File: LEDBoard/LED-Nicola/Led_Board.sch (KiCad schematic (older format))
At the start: 33 parts, among them J1 MOUNTING_HOLE, J10 CONN_01X02, J11 LED CONN 01X16, J12 CONN_01X02, J13 LED CONN 01X04, J2 MOUNTING_HOLE, J3 MOUNTING_HOLE, J4 MOUNTING_HOLE, J5 Arduino CONN 01X04, J6 Arduino CONN_01X04, J7 Arduino CONN_01X06, J8 VD 0 CONN_01X02, J9 CONN_01X02, Q1 MMBT2222ALT1G, U1 SSR

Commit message: Changes
plz let me push
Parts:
- added BZ101: Buzzer, hyperCustom:nicolaBuzzer, symbol Buzzer
- added R101, R102: R, Resistors_ThroughHole:R_Axial_DIN0309_L9.0mm_D3.2mm_P12.70mm_Horizontal, symbol R
- J11: Digikey PN (none) -> 277-1220-ND; Link (none) -> https://www.digikey.com/product-detail/en/phoenix-contact/1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
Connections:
- net 5V0: now also R102.2
- net Buzzer: now also R101.1; no longer U1.5 (LOAD)
- net GND: now also BZ101.2 (+)
- new net: R101.2, U1.5 (LOAD)
- new net: BZ101.1 (-), R102.1
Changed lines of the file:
@@
 LIBS:contrib
 LIBS:valves
-LIBS:KiCAD_Tutorial
-LIBS:5vregulatortab
-LIBS:ssr
-LIBS:SSRBoard-cache
-LIBS:SSRBoard-rescue
-LIBS:Arduino_Uno_R3_From_Scratch
-LIBS:Arduino_Uno_R3_From_Scratch-cache
-LIBS:MFN_Atmel
-LIBS:xtr117
-LIBS:mmbt2222alt1g
-LIBS:VO14642AABTR
 LIBS:Led_Board-cache
 EELAYER 25 0
@@
 F 2 "hyperCustom:CONN_PHOENIX_1844359_16PIN" H 9100 2900 50  0001 C CNN
 F 3 "" H 9100 2900 50  0001 C CNN
+F 4 "277-1220-ND" H 9100 2900 60  0001 C CNN "Digikey PN"
+F 5 "https://www.digikey.com/product-detail/en/phoenix-contact/1803413/277-1220-ND/260588" H 9100 2900 60  0001 C CNN "Link"
 	1    9100 2900
 	0    -1   -1   0
@@
 Text Label 7400 850  0    60   ~ 0
 24V
-Text Label 7450 1000 0    60   ~ 0
+Text Label 7750 1000 0    60   ~ 0
 Buzzer
 Text Label 7950 1600 2    60   ~ 0
@@
 Text Label 5950 850  2    60   ~ 0
 5V0
+$Comp
+L Buzzer BZ101
+U 1 1 597D61D1
+P 1600 5200
+F 0 "BZ101" H 1750 5250 50  0000 L CNN
+F 1 "Buzzer" H 1750 5150 50  0000 L CNN
+F 2 "hyperCustom:nicolaBuzzer" V 1575 5300 50  0001 C CNN
+F 3 "" V 1575 5300 50  0001 C CNN
+F 4 "http://www.puiaudio.com/pdf/AI-3035-TWT-3V-R.pdf" H 1600 5200 60  0001 C CNN "Link"
+	1    1600 5200
+	1    0    0    -1
+$EndComp
+Text Label 1050 5100 2    60   ~ 0
+5V0
+$Comp
+L GND #PWR101
+U 1 1 597D688D
+P 1500 5300
+F 0 "#PWR101" H 1500 5050 50  0001 C CNN
+F 1 "GND" H 1500 5150 50  0000 C CNN
+F 2 "" H 1500 5300 50  0001 C CNN
+F 3 "" H 1500 5300 50  0001 C CNN
+	1    1500 5300
+	1    0    0    -1
+$EndComp
+$Comp
+L R R102
+U 1 1 597D6C18
+P 1350 5100
+F 0 "R102" V 1430 5100 50  0000 C CNN
+F 1 "R" V 1350 5100 50  0000 C CNN
+F 2 "Resistors_ThroughHole:R_Axial_DIN0309_L9.0mm_D3.2mm_P12.70mm_Horizontal" V 1280 5100 50  0001 C CNN
+F 3 "" H 1350 5100 50  0001 C CNN
+	1    1350 5100
+	0    1    1    0
+$EndComp
+Wire Wire Line
+	1200 5100 1050 5100
+$Comp
+L R R101
+U 1 1 597D728C
+P 7600 1000
+F 0 "R101" V 7680 1000 50  0000 C CNN
+F 1 "R" V 7600 1000 50  0000 C CNN
+F 2 "Resistors_ThroughHole:R_Axial_DIN0309_L9.0mm_D3.2mm_P12.70mm_Horizontal" V 7530 1000 50  0001 C CNN
+F 3 "" H 7600 1000 50  0001 C CNN
+	1    7600 1000
+	0    1    1    0
+$EndComp
 $EndSCHEMATC

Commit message: new changes
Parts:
- removed BZ101: Buzzer, hyperCustom:nicolaBuzzer, symbol Buzzer
- removed R101, R102: R, Resistors_ThroughHole:R_Axial_DIN0309_L9.0mm_D3.2mm_P12.70mm_Horizontal, symbol R
- J11: Digikey PN 277-1220-ND -> (none); Link https://www.digikey.com/product-detail/en/phoenix-contact/1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 -> (none)
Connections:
- net Buzzer: now also U1.5 (LOAD)
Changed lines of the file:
@@
 LIBS:contrib
 LIBS:valves
+LIBS:KiCAD_Tutorial
+LIBS:5vregulatortab
+LIBS:ssr
+LIBS:SSRBoard-cache
+LIBS:SSRBoard-rescue
+LIBS:Arduino_Uno_R3_From_Scratch
+LIBS:Arduino_Uno_R3_From_Scratch-cache
+LIBS:MFN_Atmel
+LIBS:xtr117
+LIBS:mmbt2222alt1g
+LIBS:VO14642AABTR
 LIBS:Led_Board-cache
 EELAYER 25 0
@@
 F 2 "hyperCustom:CONN_PHOENIX_1844359_16PIN" H 9100 2900 50  0001 C CNN
 F 3 "" H 9100 2900 50  0001 C CNN
-F 4 "277-1220-ND" H 9100 2900 60  0001 C CNN "Digikey PN"
-F 5 "https://www.digikey.com/product-detail/en/phoenix-contact/1803413/277-1220-ND/260588" H 9100 2900 60  0001 C CNN "Link"
 	1    9100 2900
 	0    -1   -1   0
@@
 Text Label 7400 850  0    60   ~ 0
 24V
-Text Label 7750 1000 0    60   ~ 0
+Text Label 7450 1000 0    60   ~ 0
 Buzzer
 Text Label 7950 1600 2    60   ~ 0
@@
 Text Label 5950 850  2    60   ~ 0
 5V0
-$Comp
-L Buzzer BZ101
-U 1 1 597D61D1
-P 1600 5200
-F 0 "BZ101" H 1750 5250 50  0000 L CNN
-F 1 "Buzzer" H 1750 5150 50  0000 L CNN
-F 2 "hyperCustom:nicolaBuzzer" V 1575 5300 50  0001 C CNN
-F 3 "" V 1575 5300 50  0001 C CNN
-F 4 "http://www.puiaudio.com/pdf/AI-3035-TWT-3V-R.pdf" H 1600 5200 60  0001 C CNN "Link"
-	1    1600 5200
-	1    0    0    -1
-$EndComp
-Text Label 1050 5100 2    60   ~ 0
-5V0
-$Comp
-L GND #PWR101
-U 1 1 597D688D
-P 1500 5300
-F 0 "#PWR101" H 1500 5050 50  0001 C CNN
-F 1 "GND" H 1500 5150 50  0000 C CNN
-F 2 "" H 1500 5300 50  0001 C CNN
-F 3 "" H 1500 5300 50  0001 C CNN
-	1    1500 5300
-	1    0    0    -1
-$EndComp
-$Comp
-L R R102
-U 1 1 597D6C18
-P 1350 5100
-F 0 "R102" V 1430 5100 50  0000 C CNN
-F 1 "R" V 1350 5100 50  0000 C CNN
-F 2 "Resistors_ThroughHole:R_Axial_DIN0309_L9.0mm_D3.2mm_P12.70mm_Horizontal" V 1280 5100 50  0001 C CNN
-F 3 "" H 1350 5100 50  0001 C CNN
-	1    1350 5100
-	0    1    1    0
-$EndComp
-Wire Wire Line
-	1200 5100 1050 5100
-$Comp
-L R R101
-U 1 1 597D728C
-P 7600 1000
-F 0 "R101" V 7680 1000 50  0000 C CNN
-F 1 "R" V 7600 1000 50  0000 C CNN
-F 2 "Resistors_ThroughHole:R_Axial_DIN0309_L9.0mm_D3.2mm_P12.70mm_Horizontal" V 7530 1000 50  0001 C CNN
-F 3 "" H 7600 1000 50  0001 C CNN
-	1    7600 1000
-	0    1    1    0
-$EndComp
 $EndSCHEMATC

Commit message: changes
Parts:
- added BZ101: Buzzer, hyperCustom:nicolaBuzzer, symbol Buzzer
- added R101, R102: R, Resistors_ThroughHole:R_Axial_DIN0309_L9.0mm_D3.2mm_P12.70mm_Horizontal, symbol R
- J10: DigiKey PN (none) -> 277-2416-ND; Mfg.  (none) -> Phoenix; Mfg. PN (none) -> 1844210
- J11: Digikey PN (none) -> 277-6211-ND; Link (none) -> https://www.digikey.com/product-detail/en/phoenix-contact/1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; Mfg.  (none) -> Phoenix; Mfg. PN (none) -> 1828003
- J12: Digikey PN (none) -> 277-2416-ND; Mfg.  (none) -> Phoenix; Mfg. PN (none) -> 1844210
- J13, J5, J6: Digikey PN (none) -> 277-2419-ND; Mfg.  (none) -> Phoenix; Mfg. PN (none) -> 1844236
- J7: Digikey PN (none) -> 277-2427-ND; Mfg.  (none) -> Phoenix; Mfg. PN (none) -> 1844525
- J8, J9: Digikey PN (none) -> 277-2416-ND; Mfg. (none) -> Phoenix; Mfg. PN (none) -> 1844210
- Q1: Mfg. (none) -> ON Semiconductors
- U1: Digikey PN (none) -> VO14642AABCT-ND; Mfg (none) -> Vishay Semiconductor Oppto Division; Mfg. PN (none) -> VO14642AABTR
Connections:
- net 24V: now also J5.2 (P2); no longer J5.3 (P3)
- net 5V0: now also J5.3 (P3); no longer J5.4 (P4)
- net A0: now also J5.1 (P1); no longer J5.2 (P2)
- net A1: now also J6.4 (P4); no longer J5.1 (P1)
- net A2: now also J6.3 (P3); no longer J6.4 (P4)
- net A3: now also J6.2 (P2); no longer J6.3 (P3)
- net A4: now also J6.1 (P1); no longer J6.2 (P2)
- net A5: now also J7.6 (P6); no longer J6.1 (P1)
- net A6: now also J7.5 (P5); no longer J7.6 (P6)
- net A7: now also J7.4 (P4); no longer J7.5 (P5), Q1.1 (B)
- net A8: now also J7.3 (P3); no longer J7.4 (P4)
- net Buzzer: now also R101.1; no longer U1.5 (LOAD)
- net GND: now also BZ101.2 (+); no longer J7.2 (P2)
- net ArduinoLED: now reaches J7.1 (P1)
- net ArduinoLED: now also R17.2
- removed net A9: J7.3 (P3), R17.2
- new net: R101.2, U1.5 (LOAD)
- new net: BZ101.1 (-), R102.1
- new net 5V: J7.2 (P2), R102.2
- new net Transistor: J5.4 (P4), Q1.1 (B)
- no-connect marks 3 -> 2
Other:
- moved on the sheet: J5, J6, J7
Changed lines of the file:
@@
 F 2 "VO14642AABTR:SOIC254P1005X390-6N" H 6700 1000 60  0001 C CNN
 F 3 "" H 6700 1000 60  0001 C CNN
+F 4 "VO14642AABCT-ND" H 6700 1000 60  0001 C CNN "Digikey PN"
+F 5 "Vishay Semiconductor Oppto Division" H 6700 1000 60  0001 C CNN "Mfg"
+F 6 "VO14642AABTR" H 6700 1000 60  0001 C CNN "Mfg. PN"
 	1    6700 1000
 	1    0    0    -1
@@
 GND
 Text Label 5300 1350 3    60   ~ 0
-A7
+Transistor
 $Comp
 L R R7
@@
 Text Label 2850 2950 0    60   ~ 0
 A6
-Text Label 2850 3050 0    60   ~ 0
-A7
+Text Label 2600 2050 0    60   ~ 0
+Transistor
 Wire Wire Line
 	2600 3050 2850 3050
@@
 L CONN_01X04 J5
 U 1 1 5979ADB2
-P 2400 2300
-F 0 "J5" H 2500 2250 50  0000 C CNN
-F 1 "Arduino CONN 01X04" H 2850 2150 50  0000 C CNN
-F 2 "hyperCustom:CONN_PHOENIX_1844236_4PIN" H 2400 2300 50  0001 C CNN
-F 3 "" H 2400 2300 50  0001 C CNN
-	1    2400 2300
+P 2400 2200
+F 0 "J5" H 2500 2150 50  0000 C CNN
+F 1 "Arduino CONN 01X04" H 2850 2050 50  0000 C CNN
+F 2 "hyperCustom:CONN_PHOENIX_1844236_4PIN" H 2400 2200 50  0001 C CNN
+F 3 "" H 2400 2200 50  0001 C CNN
+F 4 "277-2419-ND" H 2400 2200 60  0001 C CNN "Digikey PN"
+F 5 "Phoenix" H 2400 2200 60  0001 C CNN "Mfg. "
+F 6 "1844236" H 2400 2200 60  0001 C CNN "Mfg. PN"
+	1    2400 2200
 	-1   0    0    1
 $EndComp
@@
 L CONN_01X04 J6
 U 1 1 5979AE62
-P 2400 2700
-F 0 "J6" H 2500 2650 50  0000 C CNN
-F 1 "Arduino CONN_01X04" H 2850 2550 50  0000 C CNN
-F 2 "hyperCustom:CONN_PHOENIX_1844236_4PIN" H 2400 2700 50  0001 C CNN
-F 3 "" H 2400 2700 50  0001 C CNN
-	1    2400 2700
+P 2400 2600
+F 0 "J6" H 2500 2550 50  0000 C CNN
+F 1 "Arduino CONN_01X04" H 2850 2450 50  0000 C CNN
+F 2 "hyperCustom:CONN_PHOENIX_1844236_4PIN" H 2400 2600 50  0001 C CNN
+F 3 "" H 2400 2600 50  0001 C CNN
+F 4 "277-2419-ND" H 2400 2600 60  0001 C CNN "Digikey PN"
+F 5 "Phoenix" H 2400 2600 60  0001 C CNN "Mfg. "
+F 6 "1844236" H 2400 2600 60  0001 C CNN "Mfg. PN"
+	1    2400 2600
 	-1   0    0    1
 $EndComp
@@
 F 2 "hyperCustom:CONN_PHOENIX_1844210_2PIN" H 4050 4850 50  0001 C CNN
 F 3 "" H 4050 4850 50  0001 C CNN
+F 4 "277-2416-ND" H 4050 4850 60  0001 C CNN "Digikey PN"
+F 5 "Phoenix" H 4050 4850 60  0001 C CNN "Mfg."
+F 6 "1844210" H 4050 4850 60  0001 C CNN "Mfg. PN"
 	1    4050 4850
 	0    -1   -1   0
@@
 F 2 "hyperCustom:CONN_PHOENIX_1844210_2PIN" H 4800 4850 50  0001 C CNN
 F 3 "" H 4800 4850 50  0001 C CNN
+F 4 "277-2416-ND" H 4800 4850 60  0001 C CNN "Digikey PN"
+F 5 "Phoenix" H 4800 4850 60  0001 C CNN "Mfg."
+F 6 "1844210" H 4800 4850 60  0001 C CNN "Mfg. PN"
 	1    4800 4850
 	0    -1   -1   0
@@
 F 2 "hyperCustom:CONN_PHOENIX_1844210_2PIN" H 5400 4850 50  0001 C CNN
 F 3 "" H 5400 4850 50  0001 C CNN
+F 4 "277-2416-ND" H 5400 4850 60  0001 C CNN "DigiKey PN"
+F 5 "Phoenix" H 5400 4850 60  0001 C CNN "Mfg. "
+F 6 "1844210" H 5400 4850 60  0001 C CNN "Mfg. PN"
 	1    5400 4850
 	0    -1   -1   0
@@
 Wire Wire Line
 	2600 3250 2850 3250
-Text Label 2850 3350 0    60   ~ 0
-GND
 Wire Wire Line
 	7650 4500 7650 4250
@@
 F 2 "hyperCustom:CONN_PHOENIX_1844359_16PIN" H 9100 2900 50  0001 C CNN
 F 3 "" H 9100 2900 50  0001 C CNN
+F 4 "277-6211-ND" H 9100 2900 60  0001 C CNN "Digikey PN"
+F 5 "https://www.digikey.com/product-detail/en/phoenix-contact/1803413/277-1220-ND/260588" H 9100 2900 60  0001 C CNN "Link"
+F 6 "Phoenix" H 9100 2900 60  0001 C CNN "Mfg. "
+F 7 "1828003" H 9100 2900 60  0001 C CNN "Mfg. PN"
 	1    9100 2900
 	0    -1   -1   0
@@
 F 2 "foot:MMBF170LT1G" H 5700 1350 60  0001 C CNN
 F 3 "" H 5700 1350 60  0000 C CNN
+F 4 "ON Semiconductors" H 5700 1350 60  0001 C CNN "Mfg."
 	1    5700 1350
 	1    0    0    -1
@@
 F 2 "hyperCustom:CONN_PHOENIX_1844210_2PIN" H 8400 1650 50  0001 C CNN
 F 3 "" H 8400 1650 50  0001 C CNN
+F 4 "277-2416-ND" V 8400 1650 60  0001 C CNN "Digikey PN"
+F 5 "Phoenix" V 8400 1650 60  0001 C CNN "Mfg. "
+F 6 "1844210" V 8400 1650 60  0001 C CNN "Mfg. PN"
 	1    8400 1650
 	1    0    0    -1
@@
 A8
 $Comp
-L R R17
-U 1 1 597CFDDB
-P 9800 4650
-F 0 "R17" V 9880 4650 50  0000 C CNN
-F 1 "220" V 9800 4650 50  0000 C CNN
-F 2 "Resistors_SMD:R_1206_HandSoldering" V 9730 4650 50  0001 C CNN
-F 3 "" H 9800 4650 50  0001 C CNN
-	1    9800 4650
-	1    0    0    -1
-$EndComp
-Wire Wire Line
-	9800 4500 9800 4250
-Wire Wire Line
-	9800 4800 9800 4900
-Text Label 9800 4900 0    60   ~ 0
-A9
-Text Label 9800 4250 0    60   ~ 0
-L9
-$Comp
 L CONN_01X04 J13
 U 1 1 597D049A
@@
 F 2 "hyperCustom:CONN_PHOENIX_1844236_4PIN" H 10350 2900 50  0001 C CNN
 F 3 "" H 10350 2900 50  0001 C CNN
+F 4 "277-2419-ND" H 10350 2900 60  0001 C CNN "Digikey PN"
+F 5 "Phoenix" H 10350 2900 60  0001 C CNN "Mfg. "
+F 6 "1844236" H 10350 2900 60  0001 C CNN "Mfg. PN"
 	1    10350 2900
 	0    -1   -1   0
 $EndComp
-Text Label 10400 3100 3    60   ~ 0
-L9
-Text Label 10500 3100 3    60   ~ 0
-GND
 Wire Wire Line
 	7200 1150 7300 1150
@@
 Text Label 2600 2150 0    60   ~ 0
 5V0
-Text Label 2850 3250 0    60   ~ 0
-A9
+Text Label 2850 3050 0    60   ~ 0
+A7
 Text Label 2850 3150 0    60   ~ 0
 A8
@@
 L CONN_01X06 J7
 U 1 1 597E4F88
-P 2400 3200
-F 0 "J7" H 2400 3550 50  0000 C CNN
-F 1 "Arduino CONN_01X06" H 2850 2950 50  0000 C CNN
-F 2 "hyperCustom:CONN_PHOENIX_1844252_6PIN" H 2400 3200 50  0001 C CNN
-F 3 "" H 2400 3200 50  0001 C CNN
-	1    2400 3200
+P 2400 3100
+F 0 "J7" H 2500 2950 50  0000 C CNN
+F 1 "Arduino CONN_01X06" H 2850 2850 50  0000 C CNN
+F 2 "hyperCustom:CONN_PHOENIX_1844252_6PIN" H 2400 3100 50  0001 C CNN
+F 3 "" H 2400 3100 50  0001 C CNN
+F 4 "277-2427-ND" H 2400 3100 60  0001 C CNN "Digikey PN"
+F 5 "Phoenix" H 2400 3100 60  0001 C CNN "Mfg. "
+F 6 "1844525" H 2400 3100 60  0001 C CNN "Mfg. PN"
+	1    2400 3100
 	-1   0    0    1
 $EndComp
-NoConn ~ 2600 3450
 Text Label 7400 850  0    60   ~ 0
 24V
-Text Label 7450 1000 0    60   ~ 0
+Text Label 7750 1000 0    60   ~ 0
 Buzzer
 Text Label 7950 1600 2    60   ~ 0
@@
 Text Label 5950 850  2    60   ~ 0
 5V0
+$Comp
+L Buzzer BZ101
+U 1 1 597D61D1
+P 1600 5200
+F 0 "BZ101" H 1750 5250 50  0000 L CNN
+F 1 "Buzzer" H 1750 5150 50  0000 L CNN
+F 2 "hyperCustom:nicolaBuzzer" V 1575 5300 50  0001 C CNN
+F 3 "" V 1575 5300 50  0001 C CNN
+F 4 "http://www.puiaudio.com/pdf/AI-3035-TWT-3V-R.pdf" H 1600 5200 60  0001 C CNN "Link"
+F 5 "668-1204-ND" H 1600 5200 60  0001 C CNN "Digikey PN"
+	1    1600 5200
+	1    0    0    -1
+$EndComp
+Text Label 1050 5100 2    60   ~ 0
+5V
+$Comp
+L R R102
+U 1 1 597D6C18
+P 1350 5100
+F 0 "R102" V 1430 5100 50  0000 C CNN
+F 1 "R" V 1350 5100 50  0000 C CNN
+F 2 "Resistors_ThroughHole:R_Axial_DIN0309_L9.0mm_D3.2mm_P12.70mm_Horizontal" V 1280 5100 50  0001 C CNN
+F 3 "" H 1350 5100 50  0001 C CNN
+	1    1350 5100
+	0    1    1    0
+$EndComp
+Wire Wire Line
+	1200 5100 1050 5100
+$Comp
+L R R101
+U 1 1 597D728C
+P 7600 1000
+F 0 "R101" V 7680 1000 50  0000 C CNN
+F 1 "R" V 7600 1000 50  0000 C CNN
+F 2 "Resistors_ThroughHole:R_Axial_DIN0309_L9.0mm_D3.2mm_P12.70mm_Horizontal" V 7530 1000 50  0001 C CNN
+F 3 "" H 7600 1000 50  0001 C CNN
+	1    7600 1000
+	0    1    1    0
+$EndComp
+Text Label 1500 5300 2    60   ~ 0
+GND
+Text Label 2850 3250 0    60   ~ 0
+5V
+Text Label 2850 3350 0    60   ~ 0
+ArduinoLED
+$Comp
+L R R17
+U 1 1 597EBDF6
+P 9750 4650
+F 0 "R17" V 9830 4650 50  0000 C CNN
+F 1 "220" V 9750 4650 50  0000 C CNN
+F 2 "Resistors_SMD:R_1206_HandSoldering" V 9680 4650 50  0001 C CNN
+F 3 "" H 9750 4650 50  0001 C CNN
+	1    9750 4650
+	1    0    0    -1
+$EndComp
+Text Label 9750 4250 0    60   ~ 0
+L9
+Wire Wire Line
+	9750 4500 9750 4250
+Text Label 9750 4900 0    60   ~ 0
+ArduinoLED
+Wire Wire Line
+	9750 4800 9750 4900
+Text Label 10400 3100 3    60   ~ 0
+L9
+Text Label 10500 3100 3    60   ~ 0
+GND
 $EndSCHEMATC

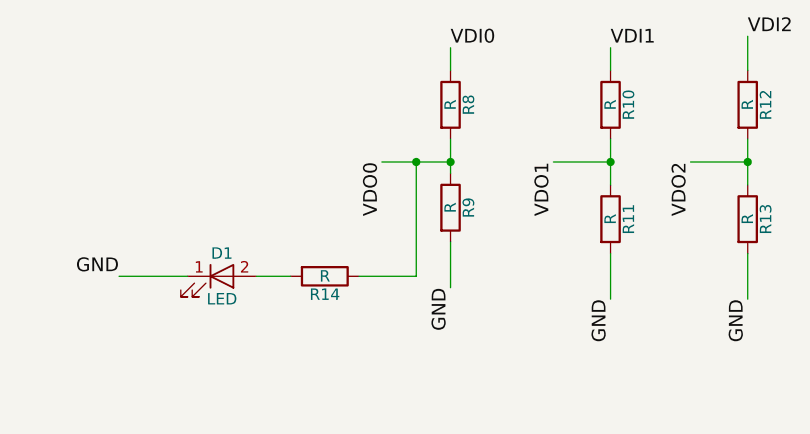
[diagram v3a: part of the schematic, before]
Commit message: Finalized LED Board
Added Silkscreen for all sides of the board and all connectors. Moved
the Placement of the Power on LED to show then the arduino is
outputting power correctly. Slightly move components to make it more
efficient.
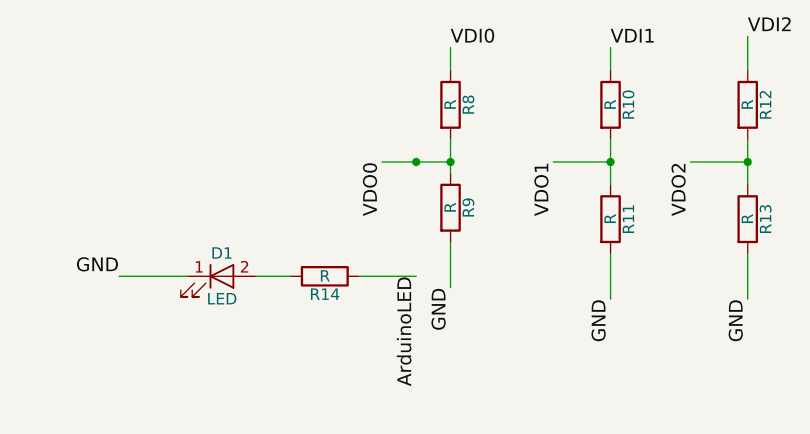
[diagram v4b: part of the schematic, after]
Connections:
- net ArduinoLED: now also R14.1
- net VDO0: no longer R14.1
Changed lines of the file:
@@
 LIBS:contrib
 LIBS:valves
-LIBS:KiCAD_Tutorial
-LIBS:5vregulatortab
-LIBS:ssr
-LIBS:SSRBoard-cache
-LIBS:SSRBoard-rescue
-LIBS:Arduino_Uno_R3_From_Scratch
-LIBS:Arduino_Uno_R3_From_Scratch-cache
-LIBS:MFN_Atmel
-LIBS:xtr117
-LIBS:mmbt2222alt1g
-LIBS:VO14642AABTR
 LIBS:Led_Board-cache
 EELAYER 25 0
@@
 	1    0    0    -1
 $EndComp
-Wire Wire Line
-	3900 6650 3900 6150
 Connection ~ 3900 6150
 Wire Wire Line
 	3200 6650 3350 6650
-$Comp
-L R R14
-U 1 1 5979C2F0
-P 3500 6650
-F 0 "R14" V 3580 6650 50  0000 C CNN
-F 1 "R" V 3500 6650 50  0000 C CNN
-F 2 "Resistors_SMD:R_1206_HandSoldering" V 3430 6650 50  0001 C CNN
-F 3 "" H 3500 6650 50  0001 C CNN
-	1    3500 6650
-	0    1    1    0
-$EndComp
-Wire Wire Line
-	3650 6650 3900 6650
 Wire Wire Line
 	2900 6650 2600 6650
@@
 Text Label 10500 3100 3    60   ~ 0
 GND
+Wire Wire Line
+	3650 6650 3900 6650
+$Comp
+L R R14
+U 1 1 5979C2F0
+P 3500 6650
+F 0 "R14" V 3580 6650 50  0000 C CNN
+F 1 "R" V 3500 6650 50  0000 C CNN
+F 2 "Resistors_SMD:R_1206_HandSoldering" V 3430 6650 50  0001 C CNN
+F 3 "" H 3500 6650 50  0001 C CNN
+	1    3500 6650
+	0    1    1    0
+$EndComp
+Text Label 3900 6650 3    60   ~ 0
+ArduinoLED
 $EndSCHEMATC
